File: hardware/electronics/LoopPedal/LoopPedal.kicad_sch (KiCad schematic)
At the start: 9 parts, among them SW1 SW_SPST, SW2 SW_SPST, SW3 SW_SPST, SW4 SW_SPST, SW5 SW_SPST, SW6 SW_SPST, SW7 SW_SPST, SW8 SW_SPST

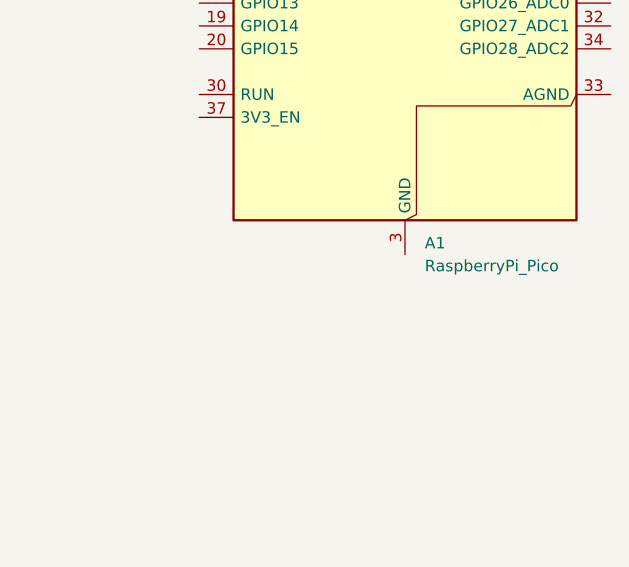
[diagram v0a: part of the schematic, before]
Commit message: adds pi pico and connectors
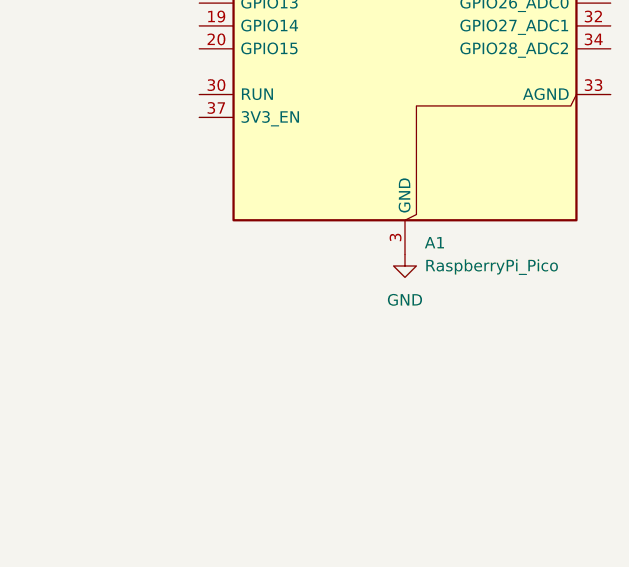
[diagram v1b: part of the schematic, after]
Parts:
- SW1, SW2, SW3, SW4, SW5, SW6, SW7, SW8: footprint (none) -> Connector_JST:JST_PH_B2B-PH-K_1x02_P2.00mm_Vertical
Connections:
- net GND: now also A1.13 (GND), A1.18 (GND), A1.23 (GND), A1.28 (GND), A1.3 (GND), A1.38 (GND), A1.8 (GND)
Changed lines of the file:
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@@
 			)
 		)
-		(property "Footprint" ""
+		(property "Footprint" "Connector_JST:JST_PH_B2B-PH-K_1x02_P2.00mm_Vertical"
 			(at 67.31 90.17 0)
 			(effects
@@
 			)
 		)
-		(property "Footprint" ""
+		(property "Footprint" "Connector_JST:JST_PH_B2B-PH-K_1x02_P2.00mm_Vertical"
 			(at 67.31 110.49 0)
 			(effects
@@
 	)
 	(symbol
+		(lib_id "power:GND")
+		(at 158.75 116.84 0)
+		(unit 1)
+		(exclude_from_sim no)
+		(in_bom yes)
+		(on_board yes)
+		(dnp no)
+		(fields_autoplaced yes)
+		(property "Reference" "#PWR02"
+			(at 158.75 123.19 0)
+			(effects
+				(font
+					(size 1.27 1.27)
+				)
+				(hide yes)
+			)
+		)
+		(property "Value" "GND"
+			(at 158.75 121.92 0)
+			(effects
+				(font
+					(size 1.27 1.27)
+				)
+			)
+		)
+		(property "Footprint" ""
+			(at 158.75 116.84 0)
+			(effects
+				(font
+					(size 1.27 1.27)
+				)
+				(hide yes)
+			)
+		)
+		(property "Datasheet" ""
+			(at 158.75 116.84 0)
+			(effects
+				(font
+					(size 1.27 1.27)
+				)
+				(hide yes)
+			)
+		)
+		(property "Description" "Power symbol creates a global label with name \"GND\" , ground"
+			(at 158.75 116.84 0)
+			(effects
+				(font
+					(size 1.27 1.27)
+				)
+				(hide yes)
+			)
+		)
+		(pin "1"
+		)
+		(instances
+			(project "LoopPedal"
+				(path "/244766d7-0742-4f12-9004-40de07200836"
+					(reference "#PWR02")
+					(unit 1)
+				)
+			)
+		)
+	)
+	(symbol
 		(lib_id "Switch:SW_SPST")
 		(at 67.31 80.01 0)
@@
 			)
 		)
-		(property "Footprint" ""
+		(property "Footprint" "Connector_JST:JST_PH_B2B-PH-K_1x02_P2.00mm_Vertical"
 			(at 67.31 80.01 0)
 			(effects
@@
 			)
 		)
-		(property "Footprint" ""
+		(property "Footprint" "Connector_JST:JST_PH_B2B-PH-K_1x02_P2.00mm_Vertical"
 			(at 67.31 120.65 0)
 			(effects
@@
 			)
 		)
-		(property "Footprint" ""
+		(property "Footprint" "Connector_JST:JST_PH_B2B-PH-K_1x02_P2.00mm_Vertical"
 			(at 67.31 140.97 0)
 			(effects
@@
 			)
 		)
-		(property "Footprint" ""
+		(property "Footprint" "Connector_JST:JST_PH_B2B-PH-K_1x02_P2.00mm_Vertical"
 			(at 67.31 130.81 0)
 			(effects
@@
 			)
 		)
-		(property "Footprint" ""
+		(property "Footprint" "Connector_JST:JST_PH_B2B-PH-K_1x02_P2.00mm_Vertical"
 			(at 67.31 100.33 0)
 			(effects
@@
 			)
 		)
-		(property "Footprint" ""
+		(property "Footprint" "Connector_JST:JST_PH_B2B-PH-K_1x02_P2.00mm_Vertical"
 			(at 67.31 69.85 0)
 			(effects
